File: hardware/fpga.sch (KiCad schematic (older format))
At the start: 60 parts, among them CON1 SD_Card_DM3BT, P10 CONN_01X01, P11 CONN_01X01, P12 CONN_01X01, P13 CONN_01X01, P14 CONN_01X01, P15 CONN_01X01, P16 CONN_01X01, P3 CONN_02X04, P4 CONN_02X04, P6 CONN_01X01, P9 CONN_01X01, Q2 DNP(RE1C002UN), SW2 SW_PUSH, U30 XC7A15T-1FTG256C, U40 W25Q32JV

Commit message: Current working version.
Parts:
- removed C250: 470n, fmcw3:C_0402b, symbol C
- removed CON1: SD_Card_DM3BT, fmcw3:DM3BT-DSF-PEJS, symbol SD_Card_DM3BT
- removed U30: XC7A15T-1FTG256C, fmcw3:FTG256, symbol XC7A15T-1FTG256C
- added C226: 47u, symbol Device:C
- added C235, C236, C237, C238, C239, C240: 4.7u, Capacitor_SMD:C_0805_2012Metric, symbol Device:C
- added C241, C242, C243, C244, C245, C246, C247: 470n, Capacitor_SMD:C_0402_1005Metric, symbol Device:C
- added J1: SD_Card, Connector_Card:microSD_HC_Hirose_DM3BT-DSF-PEJS, symbol Connector:SD_Card
- added U30: XC7A15T-FTG256, symbol FPGA_Xilinx_Artix7:XC7A15T-FTG256
- C170, C171, C174, C18, C187, C189, C190, C191, C192, C193, C197, C198, C199, C200, C201, C202, C203, C204, C205, C251, C252: footprint fmcw3:C_0402b -> Capacitor_SMD:C_0402_1005Metric; symbol C -> Device:C
- C181: footprint Capacitors_SMD:C_1210 -> Capacitor_SMD:C_1210_3225Metric; symbol C -> Device:C
- C182, C184, C196: footprint Capacitors_SMD:C_1206 -> Capacitor_SMD:C_1206_3216Metric; symbol C -> Device:C
- C183, C185, C186, C188, C194, C195: footprint fmcw3:C_0805b -> Capacitor_SMD:C_0805_2012Metric; symbol C -> Device:C
- D6: footprint fmcw3:LED_0603 -> LED_SMD:LED_0603_1608Metric; symbol LED -> Device:LED
- P10, P11, P12, P13, P14, P15, P16, P6, P9: symbol CONN_01X01 -> fmcw3-rescue:CONN_01X01
- P3, P4: footprint Pin_Headers:Pin_Header_Straight_2x04_Pitch2.54mm_SMD -> Connector_PinHeader_2.54mm:PinHeader_2x04_P2.54mm_Vertical_SMD; symbol CONN_02X04 -> Connector_Generic:Conn_02x04_Odd_Even
- Q2: symbol MOS_N_GSD -> fmcw3-rescue:MOS_N_GSD
- R109, R110, R111, R112, R114, R115, R117, R118, R130, R69, R70: symbol R -> Device:R
- SW2: symbol SW_PUSH -> fmcw3-rescue:SW_PUSH
- U40: footprint Housings_DFN_QFN:DFN-S-8-1EP_6x5mm_Pitch1.27mm -> Package_DFN_QFN:DFN-S-8-1EP_6x5mm_P1.27mm; symbol W25Q32JV -> fmcw3-rescue:W25Q32JV
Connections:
- wire segments 332 -> 494

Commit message: Dropped the 3 from the end of the project name.
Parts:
- P10, P11, P12, P13, P14, P15, P16, P6, P9: footprint fmcw3:TP_1.00 -> fmcw:TP_1.00; symbol fmcw3-rescue:CONN_01X01 -> fmcw-rescue:CONN_01X01-fmcw3-rescue
- Q2: footprint fmcw3:SOT-416 -> fmcw:SOT-416; symbol fmcw3-rescue:MOS_N_GSD -> fmcw-rescue:MOS_N_GSD-fmcw3-rescue
- R109, R110, R111, R112, R114, R115, R117, R118, R130, R69, R70: footprint fmcw3:R_0402b -> fmcw:R_0402b
- SW2: footprint fmcw3:EVP-AWBA2A -> fmcw:EVP-AWBA2A; symbol fmcw3-rescue:SW_PUSH -> fmcw-rescue:SW_PUSH-fmcw3-rescue
- U40: symbol fmcw3-rescue:W25Q32JV -> fmcw-rescue:W25Q32JV-fmcw3-rescue
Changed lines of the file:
@@
 EESchema Schematic File Version 4
-LIBS:fmcw3-cache
+LIBS:fmcw-cache
 EELAYER 26 0
 EELAYER END
@@
 F 0 "R69" V 3480 2100 50  0000 C CNN
 F 1 "DNP" V 3400 2100 50  0000 C CNN
-F 2 "fmcw3:R_0402b" V 3330 2100 30  0001 C CNN
+F 2 "fmcw:R_0402b" V 3330 2100 30  0001 C CNN
 F 3 "" H 3400 2100 30  0000 C CNN
 	1    3400 2100
@@
 F 0 "R70" V 3480 2500 50  0000 C CNN
 F 1 "0" V 3400 2500 50  0000 C CNN
-F 2 "fmcw3:R_0402b" V 3330 2500 30  0001 C CNN
+F 2 "fmcw:R_0402b" V 3330 2500 30  0001 C CNN
 F 3 "" H 3400 2500 30  0000 C CNN
 	1    3400 2500
@@
 F 0 "R109" V 2780 10150 50  0000 C CNN
 F 1 "240" V 2700 10150 50  0000 C CNN
-F 2 "fmcw3:R_0402b" V 2630 10150 30  0001 C CNN
+F 2 "fmcw:R_0402b" V 2630 10150 30  0001 C CNN
 F 3 "" H 2700 10150 30  0000 C CNN
 	1    2700 10150
@@
 	14350 3650 14250 3650
 $Comp
-L fmcw3-rescue:CONN_01X01 P9
+L fmcw-rescue:CONN_01X01-fmcw3-rescue P9
 U 1 1 58552888
 P 9100 8300
 F 0 "P9" H 9100 8400 50  0000 C CNN
 F 1 "CONN_01X01" V 9200 8300 50  0000 C CNN
-F 2 "fmcw3:TP_1.00" H 9100 8300 60  0001 C CNN
+F 2 "fmcw:TP_1.00" H 9100 8300 60  0001 C CNN
 F 3 "" H 9100 8300 60  0000 C CNN
 	1    9100 8300
@@
 F 0 "R114" V 9830 8700 50  0000 C CNN
 F 1 "0" V 9750 8700 50  0000 C CNN
-F 2 "fmcw3:R_0402b" V 9680 8700 30  0001 C CNN
+F 2 "fmcw:R_0402b" V 9680 8700 30  0001 C CNN
 F 3 "" H 9750 8700 30  0000 C CNN
 	1    9750 8700
@@
 F 0 "R115" V 9580 8700 50  0000 C CNN
 F 1 "0" V 9500 8700 50  0000 C CNN
-F 2 "fmcw3:R_0402b" V 9430 8700 30  0001 C CNN
+F 2 "fmcw:R_0402b" V 9430 8700 30  0001 C CNN
 F 3 "" H 9500 8700 30  0000 C CNN
 	1    9500 8700
@@
 F 0 "R110" V 10080 8700 50  0000 C CNN
 F 1 "DNP" V 10000 8700 50  0000 C CNN
-F 2 "fmcw3:R_0402b" V 9930 8700 30  0001 C CNN
+F 2 "fmcw:R_0402b" V 9930 8700 30  0001 C CNN
 F 3 "" H 10000 8700 30  0000 C CNN
 	1    10000 8700
@@
 3V3D
 $Comp
-L fmcw3-rescue:CONN_01X01 P10
+L fmcw-rescue:CONN_01X01-fmcw3-rescue P10
 U 1 1 58555ED5
 P 9000 7800
 F 0 "P10" H 9000 7900 50  0000 C CNN
 F 1 "CONN_01X01" V 9100 7800 50  0000 C CNN
-F 2 "fmcw3:TP_1.00" H 9000 7800 60  0001 C CNN
+F 2 "fmcw:TP_1.00" H 9000 7800 60  0001 C CNN
 F 3 "" H 9000 7800 60  0000 C CNN
 	1    9000 7800
@@
 	8000 8500 8150 8500
 $Comp
-L fmcw3-rescue:SW_PUSH SW2
+L fmcw-rescue:SW_PUSH-fmcw3-rescue SW2
 U 1 1 5855D765
 P 3600 10450
 F 0 "SW2" H 3750 10560 50  0000 C CNN
 F 1 "SW_PUSH" H 3600 10370 50  0000 C CNN
-F 2 "fmcw3:EVP-AWBA2A" H 3600 10450 60  0001 C CNN
+F 2 "fmcw:EVP-AWBA2A" H 3600 10450 60  0001 C CNN
 F 3 "" H 3600 10450 60  0000 C CNN
 	1    3600 10450
@@
 F 0 "R112" V 3680 9800 50  0000 C CNN
 F 1 "4.7k" V 3600 9800 50  0000 C CNN
-F 2 "fmcw3:R_0402b" V 3530 9800 30  0001 C CNN
+F 2 "fmcw:R_0402b" V 3530 9800 30  0001 C CNN
 F 3 "" H 3600 9800 30  0000 C CNN
 	1    3600 9800
@@
 F 0 "R117" V 4230 9800 50  0000 C CNN
 F 1 "4.7k" V 4150 9800 50  0000 C CNN
-F 2 "fmcw3:R_0402b" V 4080 9800 30  0001 C CNN
+F 2 "fmcw:R_0402b" V 4080 9800 30  0001 C CNN
 F 3 "" H 4150 9800 30  0000 C CNN
 	1    4150 9800
@@
 F 0 "R111" V 8930 8100 50  0000 C CNN
 F 1 "1k" V 8850 8100 50  0000 C CNN
-F 2 "fmcw3:R_0402b" V 8780 8100 30  0001 C CNN
+F 2 "fmcw:R_0402b" V 8780 8100 30  0001 C CNN
 F 3 "" H 8850 8100 30  0000 C CNN
 	1    8850 8100
@@
 3V3D
 $Comp
-L fmcw3-rescue:W25Q32JV U40
+L fmcw-rescue:W25Q32JV-fmcw3-rescue U40
 U 1 1 5856F3E8
 P 6750 10500
@@
 F 0 "R118" V 5980 10150 50  0000 C CNN
 F 1 "4.7k" V 5900 10150 50  0000 C CNN
-F 2 "fmcw3:R_0402b" V 5830 10150 30  0001 C CNN
+F 2 "fmcw:R_0402b" V 5830 10150 30  0001 C CNN
 F 3 "" H 5900 10150 30  0000 C CNN
 	1    5900 10150
@@
 	5900 10550 6050 10550
 $Comp
-L fmcw3-rescue:CONN_01X01 P11
+L fmcw-rescue:CONN_01X01-fmcw3-rescue P11
 U 1 1 58586E89
 P 3300 1500
 F 0 "P11" H 3300 1600 50  0000 C CNN
 F 1 "CONN_01X01" V 3400 1500 50  0000 C CNN
-F 2 "fmcw3:TP_1.00" H 3300 1500 60  0001 C CNN
+F 2 "fmcw:TP_1.00" H 3300 1500 60  0001 C CNN
 F 3 "" H 3300 1500 60  0000 C CNN
 	1    3300 1500
@@
 $EndComp
 $Comp
-L fmcw3-rescue:CONN_01X01 P12
+L fmcw-rescue:CONN_01X01-fmcw3-rescue P12
 U 1 1 58587941
 P 3650 1600
 F 0 "P12" H 3650 1700 50  0000 C CNN
 F 1 "CONN_01X01" V 3750 1600 50  0000 C CNN
-F 2 "fmcw3:TP_1.00" H 3650 1600 60  0001 C CNN
+F 2 "fmcw:TP_1.00" H 3650 1600 60  0001 C CNN
 F 3 "" H 3650 1600 60  0000 C CNN
 	1    3650 1600
@@
 $EndComp
 $Comp
-L fmcw3-rescue:CONN_01X01 P15
+L fmcw-rescue:CONN_01X01-fmcw3-rescue P15
 U 1 1 585708F8
 P 8750 7600
 F 0 "P15" H 8750 7700 50  0000 C CNN
 F 1 "CONN_01X01" V 8850 7600 50  0000 C CNN
-F 2 "fmcw3:TP_1.00" H 8750 7600 60  0001 C CNN
+F 2 "fmcw:TP_1.00" H 8750 7600 60  0001 C CNN
 F 3 "" H 8750 7600 60  0000 C CNN
 	1    8750 7600
@@
 $EndComp
 $Comp
-L fmcw3-rescue:CONN_01X01 P13
+L fmcw-rescue:CONN_01X01-fmcw3-rescue P13
 U 1 1 58570DB4
 P 8750 7300
 F 0 "P13" H 8750 7400 50  0000 C CNN
 F 1 "CONN_01X01" V 8850 7300 50  0000 C CNN
-F 2 "fmcw3:TP_1.00" H 8750 7300 60  0001 C CNN
+F 2 "fmcw:TP_1.00" H 8750 7300 60  0001 C CNN
 F 3 "" H 8750 7300 60  0000 C CNN
 	1    8750 7300
@@
 $EndComp
 $Comp
-L fmcw3-rescue:CONN_01X01 P16
+L fmcw-rescue:CONN_01X01-fmcw3-rescue P16
 U 1 1 58571070
 P 8500 7400
 F 0 "P16" H 8500 7500 50  0000 C CNN
 F 1 "CONN_01X01" V 8600 7400 50  0000 C CNN
-F 2 "fmcw3:TP_1.00" H 8500 7400 60  0001 C CNN
+F 2 "fmcw:TP_1.00" H 8500 7400 60  0001 C CNN
 F 3 "" H 8500 7400 60  0000 C CNN
 	1    8500 7400
@@
 $EndComp
 $Comp
-L fmcw3-rescue:CONN_01X01 P14
+L fmcw-rescue:CONN_01X01-fmcw3-rescue P14
 U 1 1 58571241
 P 9200 7500
 F 0 "P14" H 9200 7600 50  0000 C CNN
 F 1 "CONN_01X01" V 9300 7500 50  0000 C CNN
-F 2 "fmcw3:TP_1.00" H 9200 7500 60  0001 C CNN
+F 2 "fmcw:TP_1.00" H 9200 7500 60  0001 C CNN
 F 3 "" H 9200 7500 60  0000 C CNN
 	1    9200 7500
@@
 F 0 "R130" V 9680 3050 50  0000 C CNN
 F 1 "33" V 9600 3050 50  0000 C CNN
-F 2 "fmcw3:R_0402b" V 9530 3050 30  0001 C CNN
+F 2 "fmcw:R_0402b" V 9530 3050 30  0001 C CNN
 F 3 "" H 9600 3050 30  0000 C CNN
 	1    9600 3050
@@
 EXT2_6
 $Comp
-L fmcw3-rescue:MOS_N_GSD Q2
+L fmcw-rescue:MOS_N_GSD-fmcw3-rescue Q2
 U 1 1 597530AB
 P 4850 10550
 F 0 "Q2" H 4860 10720 60  0000 R CNN
 F 1 "DNP(RE1C002UN)" H 4860 10400 60  0000 R CNN
-F 2 "fmcw3:SOT-416" H 4850 10550 60  0001 C CNN
+F 2 "fmcw:SOT-416" H 4850 10550 60  0001 C CNN
 F 3 "https://www.rohm.com/datasheet/RE1C002UN/re1c002untcl-e" H 4850 10550 60  0001 C CNN
 	1    4850 10550
@@
 	8450 3300 8350 3300
 $Comp
-L fmcw3-rescue:CONN_01X01 P6
+L fmcw-rescue:CONN_01X01-fmcw3-rescue P6
 U 1 1 597918E9
 P 14950 3250
 F 0 "P6" H 14950 3350 50  0000 C CNN
 F 1 "CONN_01X01" V 15050 3250 50  0000 C CNN
-F 2 "fmcw3:TP_1.00" H 14950 3250 60  0001 C CNN
+F 2 "fmcw:TP_1.00" H 14950 3250 60  0001 C CNN
 F 3 "" H 14950 3250 60  0000 C CNN
 	1    14950 3250
@@
 	1800 6850 1000 6850
 $Comp
-L fmcw3-rescue:GND #PWR015
+L fmcw-rescue:GND-fmcw3-rescue #PWR015
 U 1 1 5B87ABA4
 P 800 6850

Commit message: Adjusted power supply for new power amplifier.
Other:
- note added: "5 mA"
- note added: "78 mA"
- note added: "Iq: 1 mA\nIon: 201 mA"
- note added: "Iq: 10 uA\nIon: 20 mA"
- note added: "Iq: 2 mA\nIon: 62 mA"
- note added: "Iq: 22 mA\nIon: 62 mA"
- note added: "Iq: 95 mA\nIon: 215 mA"
- note added: "Power-on current\n1V0: 277 mA\n1V8: 62 mA\n3V3: 296 mA\n3V6: 78 mA"
- note added: "Quiescent current\n1V0: 97 mA\n1V8: 22 mA\n3V3: 71 mA\n3V6: 78 mA"
- note removed: "1 mA"
- note removed: "80 mA"
- note removed: "Power-on current\n1V0: Iq + 180 mA\n1V8: Iq + 40 mA\n3V3: Iq + 40 mA"
- note removed: "Quiescent current\n1V0: 97 mA\n1V8: 22 mA\n3V3: 2 mA"
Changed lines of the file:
@@
 EESchema Schematic File Version 4
 LIBS:fmcw-cache
-EELAYER 29 0
+EELAYER 26 0
 EELAYER END
 $Descr A3 16535 11693
@@
 Wire Wire Line
 	11650 8950 11600 8950
-Text Notes 2000 5500 0    60   ~ 0
-Quiescent current\n1V0: 97 mA\n1V8: 22 mA\n3V3: 2 mA
-Text Notes 2950 5500 0    60   ~ 0
-Power-on current\n1V0: Iq + 180 mA\n1V8: Iq + 40 mA\n3V3: Iq + 40 mA
+Text Notes 2000 5600 0    60   ~ 0
+Quiescent current\n1V0: 97 mA\n1V8: 22 mA\n3V3: 71 mA\n3V6: 78 mA
+Text Notes 2950 5600 0    60   ~ 0
+Power-on current\n1V0: 277 mA\n1V8: 62 mA\n3V3: 296 mA\n3V6: 78 mA
 Text Notes 2000 5050 0    60   ~ 0
 Power supply ramp time: 0.2 ms - 50 ms
 Wire Wire Line
 	8350 5700 8450 5700
-Text Notes 1700 3100 0    60   ~ 0
-80 mA
+Text Notes 1700 3100 0    50   ~ 0
+78 mA
 Wire Wire Line
 	1400 3050 1150 3050
@@
 Text Notes 1650 800  0    60   ~ 0
 70 mA
-Text Notes 1700 3000 0    60   ~ 0
-1 mA
+Text Notes 1750 3000 0    50   ~ 0
+5 mA
 Wire Wire Line
 	9150 10700 9050 10700
@@
 Wire Wire Line
 	14150 8100 13900 8100
+Text Notes 4100 6750 0    50   ~ 0
+Iq: 95 mA\nIon: 215 mA
+Text Notes 1600 7450 0    50   ~ 0
+Iq: 2 mA\nIon: 62 mA
+Text Notes 1100 6550 0    50   ~ 0
+Iq: 22 mA\nIon: 62 mA
+Text Notes 8250 850  0    50   ~ 0
+Iq: 1 mA\nIon: 201 mA
+Text Notes 6950 10000 0    50   ~ 0
+Iq: 10 uA\nIon: 20 mA
 $EndSCHEMATC

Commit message: Documentation for TPS5420D buck converter.
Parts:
- C170, C171, C187, C189, C190, C191, C192, C193, C197, C198, C199, C200, C201, C202, C203, C204, C205, C241, C242, C243, C244, C245, C246, C247, C251: footprint Capacitor_SMD:C_0402_1005Metric -> Capacitor_SMD:C_0603_1608Metric; MFN (none) -> GRM188R70J474KA01
- C181: MFN (none) -> GRM32ER60J107ME20L
- C182: MFN (none) -> C3216JB1C476M160AB
- C183, C185, C186, C188, C194, C195, C235, C236, C237, C238, C239, C240: MFN (none) -> CL21A475KLCLQNC
- C226: footprint (none) -> Capacitor_SMD:C_1210_3225Metric; MFN (none) -> C3216JB1C476M160AB
- U40: MFN (none) -> W25Q32JVZPIQ

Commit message: Added MFNs to components.
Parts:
- removed P10, P11, P12, P13, P14, P15, P16, P6, P9: CONN_01X01, fmcw:TP_1.00, symbol fmcw-rescue:CONN_01X01-fmcw3-rescue
- added TP1, TP2, TP3, TP4, TP5, TP6, TP7, TP8, TP9: TestPoint, TestPoint:TestPoint_Pad_D1.0mm, symbol Connector:TestPoint
- C18, C252: MFN (none) -> CL05B104KO5NNNC
- C184, C196: MFN (none) -> C3216JB1C476M160AB
- D6: value LED -> Red; MFN (none) -> SML-D12V8WT86
- J1: symbol Connector:SD_Card -> Connector:Micro_SD_Card_Det_Hirose_DM3AT; MFN (none) -> DM3BT-DSF-PEJS
- P3, P4: MFN (none) -> 95278-101A08LF
- Q2: footprint fmcw:SOT-416 -> Package_TO_SOT_SMD:SOT-416; symbol fmcw-rescue:MOS_N_GSD-fmcw3-rescue -> Device:Q_NMOS_GSD
- R109: footprint fmcw:R_0402b -> Resistor_SMD:R_0402_1005Metric; MFN (none) -> ERJ-2RKF2400X
- R110, R69: footprint fmcw:R_0402b -> Resistor_SMD:R_0402_1005Metric
- R111: footprint fmcw:R_0402b -> Resistor_SMD:R_0402_1005Metric; MFN (none) -> ERJ-2RKF1001X
- R112, R117, R118: footprint fmcw:R_0402b -> Resistor_SMD:R_0402_1005Metric; MFN (none) -> ERJ-2GEJ472X
- R114, R115, R70: footprint fmcw:R_0402b -> Resistor_SMD:R_0402_1005Metric; MFN (none) -> ERJ-2GE0R00X
- R130: footprint fmcw:R_0402b -> Resistor_SMD:R_0402_1005Metric; MFN (none) -> ERJ-2GEJ330X
- SW2: MFN (none) -> EVP-AWBD2A
- U30: footprint (none) -> fmcw:FTG256; MFN (none) -> XC7A15T-1FTG256C
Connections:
- wire segments 494 -> 500

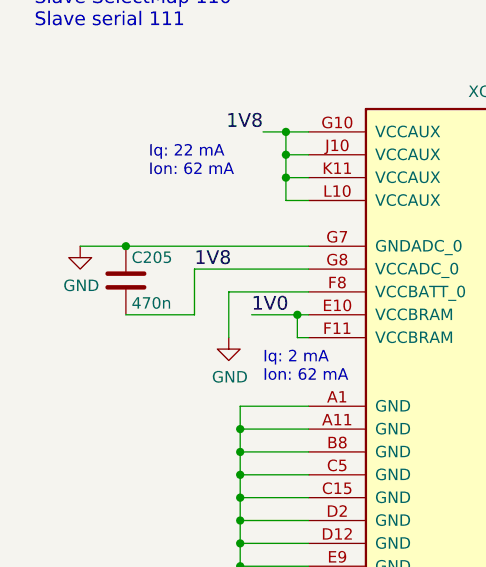
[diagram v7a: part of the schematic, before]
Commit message: Improved documentation and added schematics to default libraries.
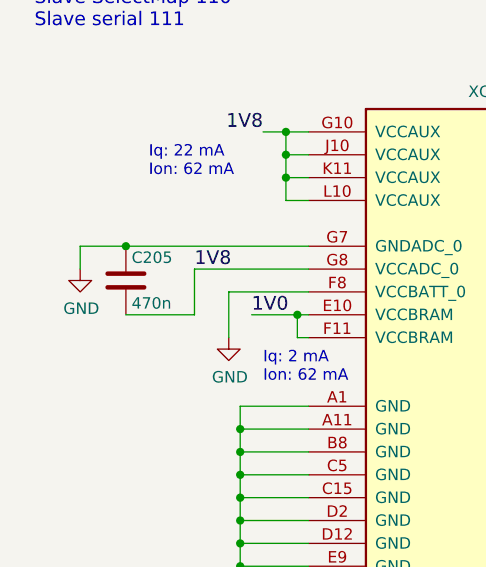
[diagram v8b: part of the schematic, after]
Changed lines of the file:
@@
 U 1 1 5B9D6CE1
 P 6350 3500
+AR Path="/5B9D6CE1" Ref="U30"  Part="1"
+AR Path="/59395D6A/5B9D6CE1" Ref="U30"  Part="1"
 F 0 "U30" H 6350 3500 50  0000 C CNN
 F 1 "XC7A15T-FTG256" H 6350 435 50  0000 C CNN
@@
 U 2 1 5CE2C3EB
 P 12250 3750
+AR Path="/5CE2C3EB" Ref="U30"  Part="2"
+AR Path="/59395D6A/5CE2C3EB" Ref="U30"  Part="2"
 F 0 "U30" H 12250 776 50  0000 C CNN
 F 1 "XC7A15T-FTG256" H 12250 685 50  0000 C CNN
@@
 U 3 1 5CE2C527
 P 6500 8100
+AR Path="/5CE2C527" Ref="U30"  Part="3"
+AR Path="/59395D6A/5CE2C527" Ref="U30"  Part="3"
 F 0 "U30" H 6550 8100 50  0000 R CNN
 F 1 "XC7A15T-FTG256" H 6800 8000 50  0000 R CNN
@@
 U 4 1 5CE2C6D0
 P 2800 7650
+AR Path="/5CE2C6D0" Ref="U30"  Part="4"
+AR Path="/59395D6A/5CE2C6D0" Ref="U30"  Part="4"
 F 0 "U30" H 2800 9217 50  0000 C CNN
 F 1 "XC7A15T-FTG256" H 2800 9126 50  0000 C CNN
@@
 Wire Wire Line
 	1800 6850 1000 6850
-$Comp
-L fmcw-rescue:GND-fmcw3-rescue #PWR015
-U 1 1 5B87ABA4
-P 800 6850
-F 0 "#PWR015" H 800 6600 50  0001 C CNN
-F 1 "GND" H 805 6677 50  0000 C CNN
-F 2 "" H 800 6850 50  0001 C CNN
-F 3 "" H 800 6850 50  0001 C CNN
-	1    800  6850
-	1    0    0    -1
-$EndComp
 Connection ~ 1000 6850
 Wire Wire Line
@@
 Wire Wire Line
 	9150 11000 9150 10900
+Wire Wire Line
+	800  6850 800  6950
+$Comp
+L power:GND #PWR?
+U 1 1 5CB5CBFC
+P 800 6950
+F 0 "#PWR?" H 800 6700 50  0001 C CNN
+F 1 "GND" H 805 6777 50  0000 C CNN
+F 2 "" H 800 6950 50  0001 C CNN
+F 3 "" H 800 6950 50  0001 C CNN
+	1    800  6950
+	1    0    0    -1
+$EndComp
 $EndSCHEMATC
